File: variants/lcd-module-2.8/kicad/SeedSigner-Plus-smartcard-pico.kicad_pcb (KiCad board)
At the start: 2 copper layers, 137.9 x 108.6 mm, 58 parts, among them J301 TYPE-C 6P(073), J302 Conn_01x02_Pin, J401 62684-402100ALF, J601 7312P0225A13LF, J701 Pico-ResTouch-LCD-2.8, Q401 AO3400A, SW501 TS-1101-C-W, SW502 TS-1101-C-W, SW503 TS-1101-C-W, SW504 TS-1101-C-W, SW505 TS-1101-C-W, SW506 TS-1101-C-W, SW507 TS-1101-C-W, SW508 TS-1101-C-W, U202 LuckFox_Pico_MINI, U601 SEC1210/PV-UR2

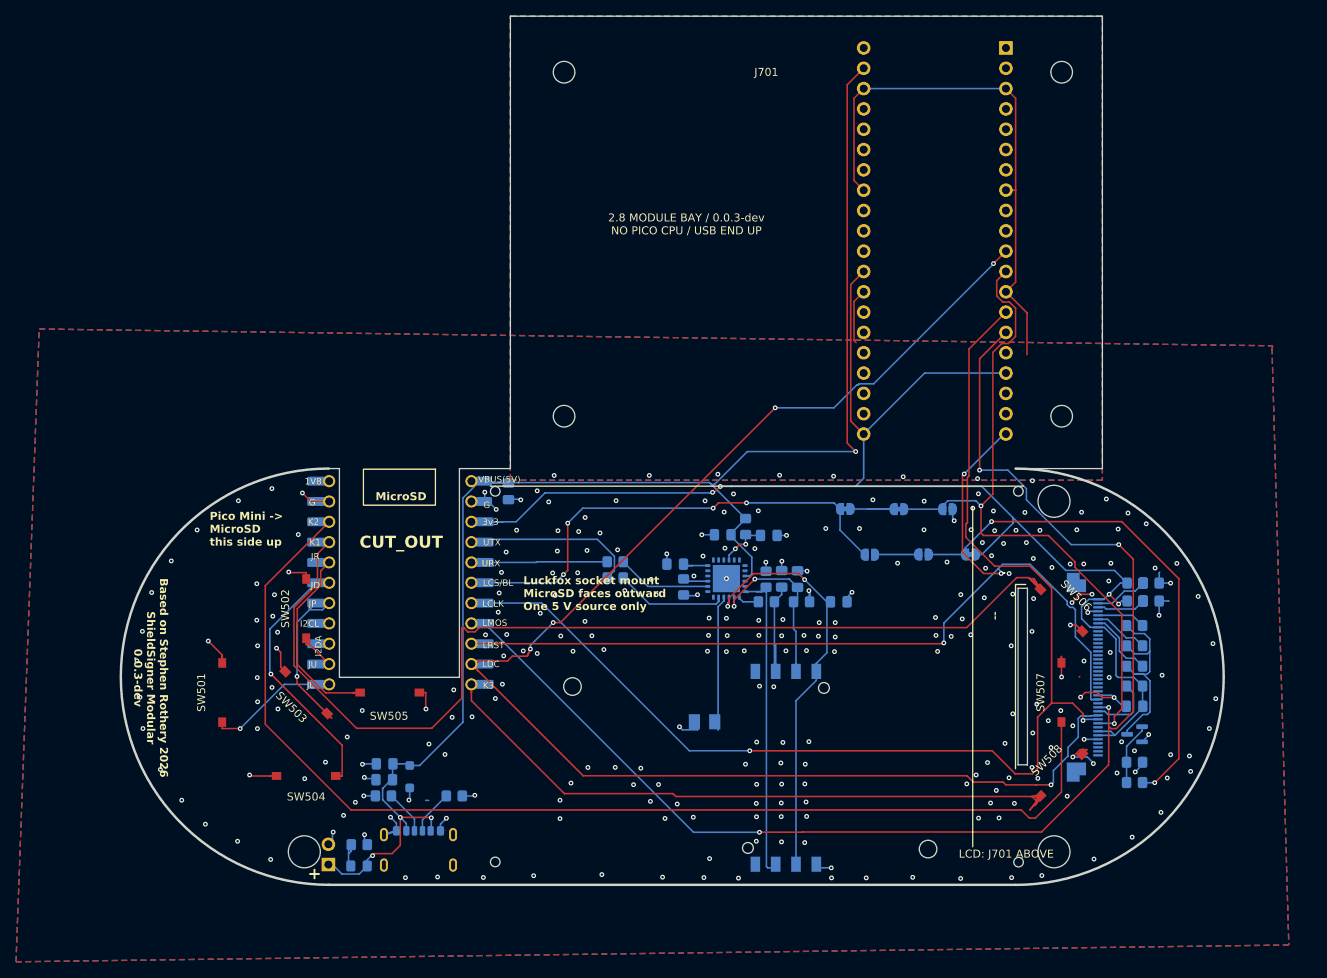
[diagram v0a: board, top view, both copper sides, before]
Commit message: Rebuild modular signer as an eight-pin 2.8-inch pill carrier
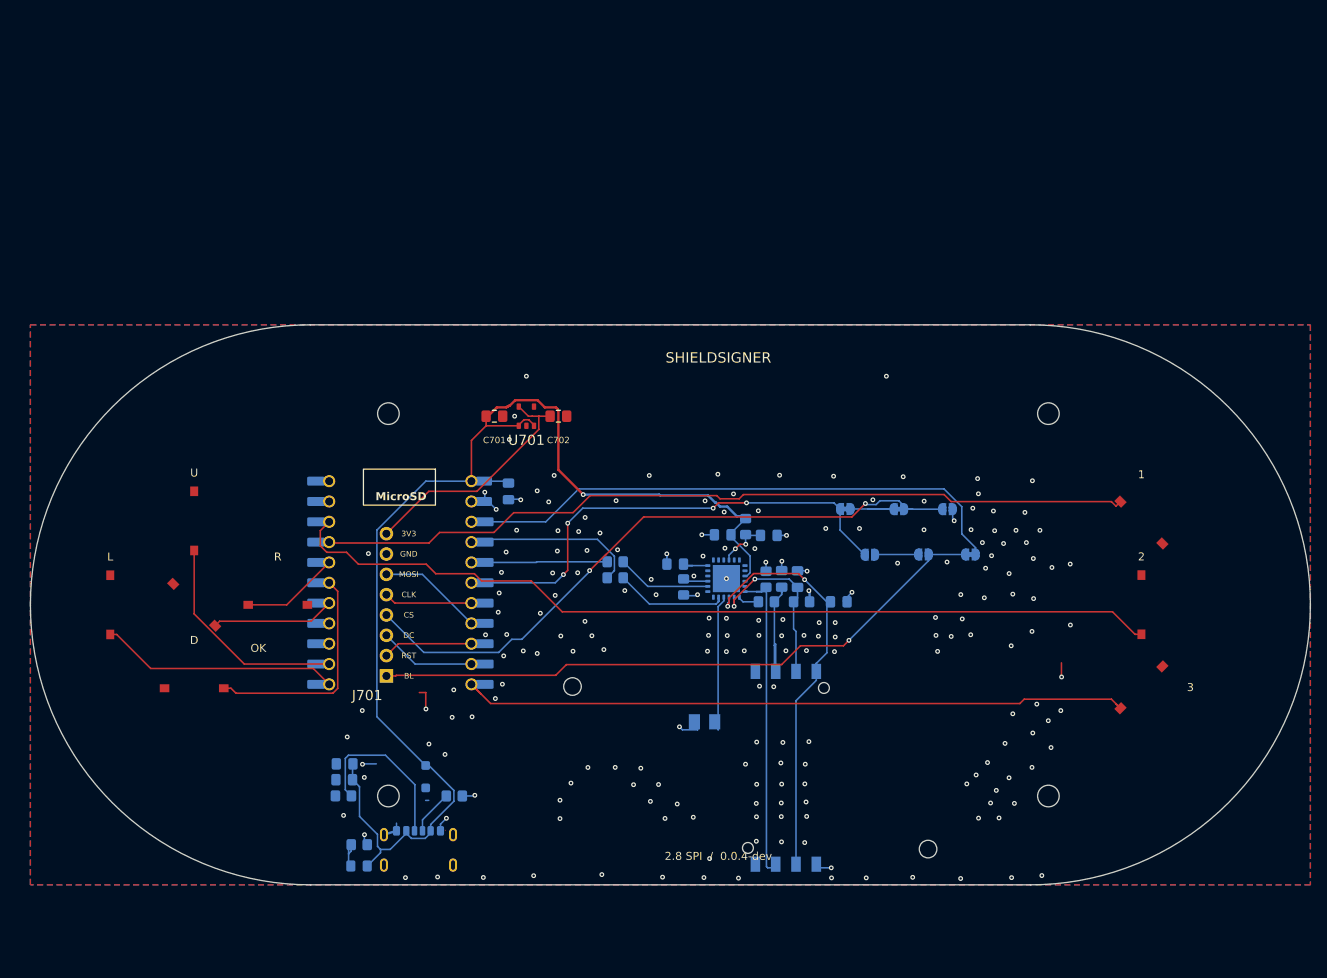
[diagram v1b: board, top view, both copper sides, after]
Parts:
- removed C401: 100n, Capacitor_SMD:C_0805_2012Metric_Pad1.18x1.45mm_HandSolder
- removed J302: Conn_01x02_Pin, Connector_PinSocket_2.54mm:PinSocket_1x02_P2.54mm_Vertical
- removed J401: 62684-402100ALF, Seedsigner-plus-library:AMPHENOL_62684-402100ALF
- removed Q401: AO3400A, Package_TO_SOT_SMD:SOT-23
- removed R401: 330R, Resistor_SMD:R_0805_2012Metric_Pad1.20x1.40mm_HandSolder
- removed R402: 33k, Resistor_SMD:R_0805_2012Metric_Pad1.20x1.40mm_HandSolder
- removed R403, R404, R408, R409: 0R, Resistor_SMD:R_0805_2012Metric_Pad1.20x1.40mm_HandSolder
- removed R405, R406, R407: 47R, Resistor_SMD:R_0805_2012Metric_Pad1.20x1.40mm_HandSolder
- removed R410: 10K, Resistor_SMD:R_0805_2012Metric_Pad1.20x1.40mm_HandSolder
- added C701: 10uF, Capacitor_SMD:C_0805_2012Metric_Pad1.18x1.45mm_HandSolder, F.Cu at (106.0, 66.0)
- added C702: 10uF, Capacitor_SMD:C_0805_2012Metric_Pad1.18x1.45mm_HandSolder, F.Cu at (114.0, 66.0)
- added U701: AP2112K-3.3TRG1, ShieldSigner:AP2112K_SOT25_reflow, F.Cu at (110.0, 66.0)
- H701, H702, H703, H704: footprint MountingHole_2.7mm_M2.5 -> MountingHole:MountingHole_2.7mm_M2.5
- J701: value Pico-ResTouch-LCD-2.8 -> LCD SPI 8-pin; footprint ShieldSigner:Waveshare_Pico_ResTouch_LCD_2.8_Header -> ShieldSigner:LCD_SPI_8_Pill
- moved J701 98.6 mm to (92.5, 98.5)
- moved H703 52.3 mm to (92.8, 113.5)
- moved H701 48.0 mm to (92.8, 65.7)
- moved H704 47.5 mm to (175.2, 113.5)
- moved H702 42.7 mm to (175.2, 65.7)
- moved SW501 17.8 mm to (58.0, 89.6)
- moved SW502 17.8 mm to (68.5, 79.1)
- moved SW503 17.8 mm to (68.5, 89.6)
- moved SW504 17.8 mm to (68.5, 100.0)
- moved SW505 17.8 mm to (78.9, 89.6)
- moved SW506 14.8 mm to (186.9, 79.3)
- moved SW507 14.8 mm to (186.9, 89.6)
- moved SW508 14.8 mm to (186.9, 99.9)
- moved C301 5.00 mm to (87.2, 111.4)
- moved C302 5.00 mm to (87.3, 109.5)
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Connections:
- J701 pad 1: unconnected-(J701-NC-Pad1) -> RPI_BACKLIGHT
- J701 pad 2: unconnected-(J701-NC-Pad2) -> LCD_RST
- J701 pad 3: GND -> LCD_DC
- J701 pad 4: unconnected-(J701-NC-Pad4) -> RPI_SPI_CS
- J701 pad 5: unconnected-(J701-NC-Pad5) -> LCD_SCLK
- J701 pad 6: unconnected-(J701-NC-Pad6) -> LCD_MOSI
- J701 pad 7: unconnected-(J701-NC-Pad7) -> GND
- J701 pad 8: GND -> LCD_3V3
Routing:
- net LCD_DC: track 183.1 -> 13.8 mm, vias 5 -> 0
- net LCD_MOSI: track 169.6 -> 14.8 mm, vias 4 -> 0
- net LCD_SCLK: track 154.1 -> 12.7 mm, vias 2 -> 0
- net GND: track 175.4 -> 39.6 mm, vias 283 -> 206
- net +3.3V: track 186.2 -> 71.0 mm, vias 4 -> 0
- net LCD_RST: track 122.1 -> 12.9 mm, vias 3 -> 0
- net Key1: track 146.2 -> 104.3 mm
- net +5V: track 192.3 -> 154.0 mm, vias 4 -> 1
- net Key2: track 144.7 -> 112.3 mm
- net LCD_3V3: track 0.00 -> 30.5 mm
- net Net-(Q401-D): track 26.1 -> 0.00 mm
- net JoystickUp: track 8.14 -> 29.0 mm
- net Net-(J301-CC2): track 5.56 -> 21.4 mm
- net JoystickLeft: track 16.5 -> 31.6 mm, vias 1 -> 0
- net RPI_BACKLIGHT: track 65.1 -> 79.1 mm, vias 2 -> 1
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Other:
- board size 137.9 x 108.6 mm -> 160 x 70 mm
- board text added: "1"
- board text added: "12 mm LCD supports"
- board text added: "2"
- board text added: "2.8 SPI / 0.0.4-dev"
- board text added: "3"
- board text added: "3V3"
- board text added: "BL"
- board text added: "Based on Stephen Rothery 2026"
- board text added: "CLK"
- board text added: "CS"
- board text added: "D"
- board text added: "DC"
- board text added: "GND"
- board text added: "L"
- board text added: "MOSI"
- board text added: "OK"
- board text added: "R"
- board text added: "RST"
- board text added: "SHIELDSIGNER"
- board text added: "U"

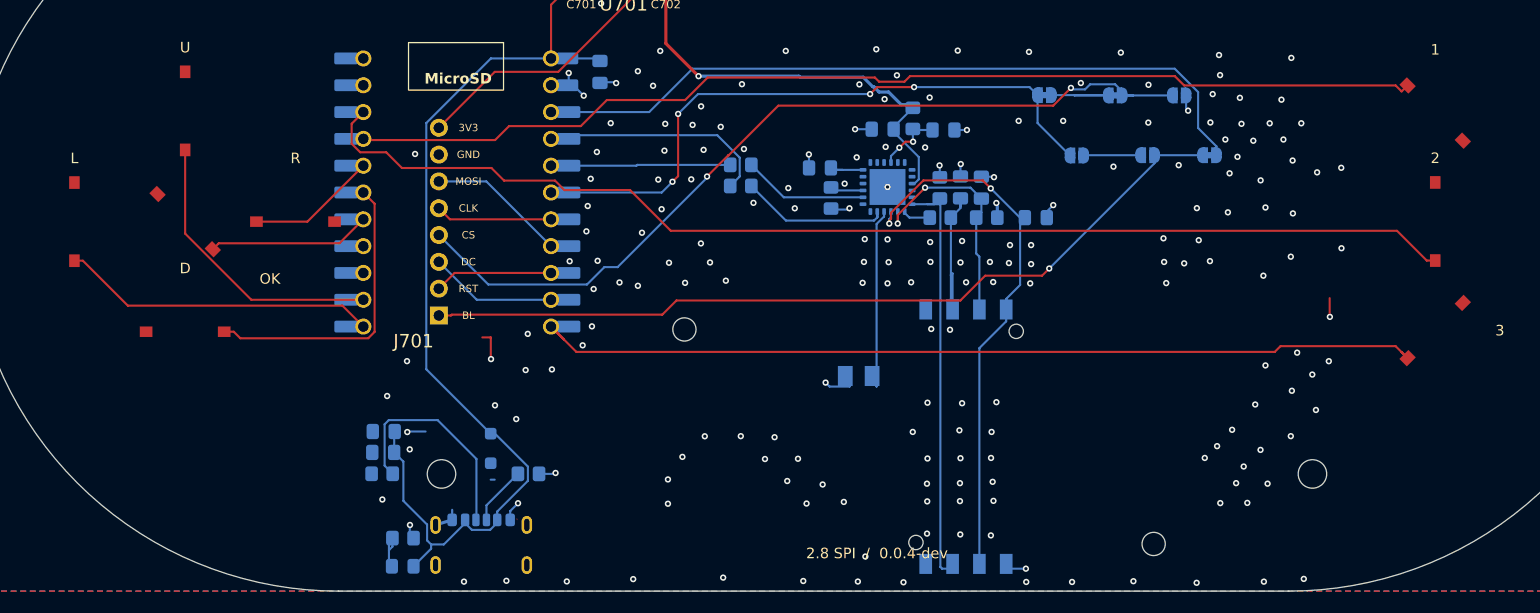
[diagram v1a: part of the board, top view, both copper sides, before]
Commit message: Revise modular carrier for shared-supplier switches and USB-C
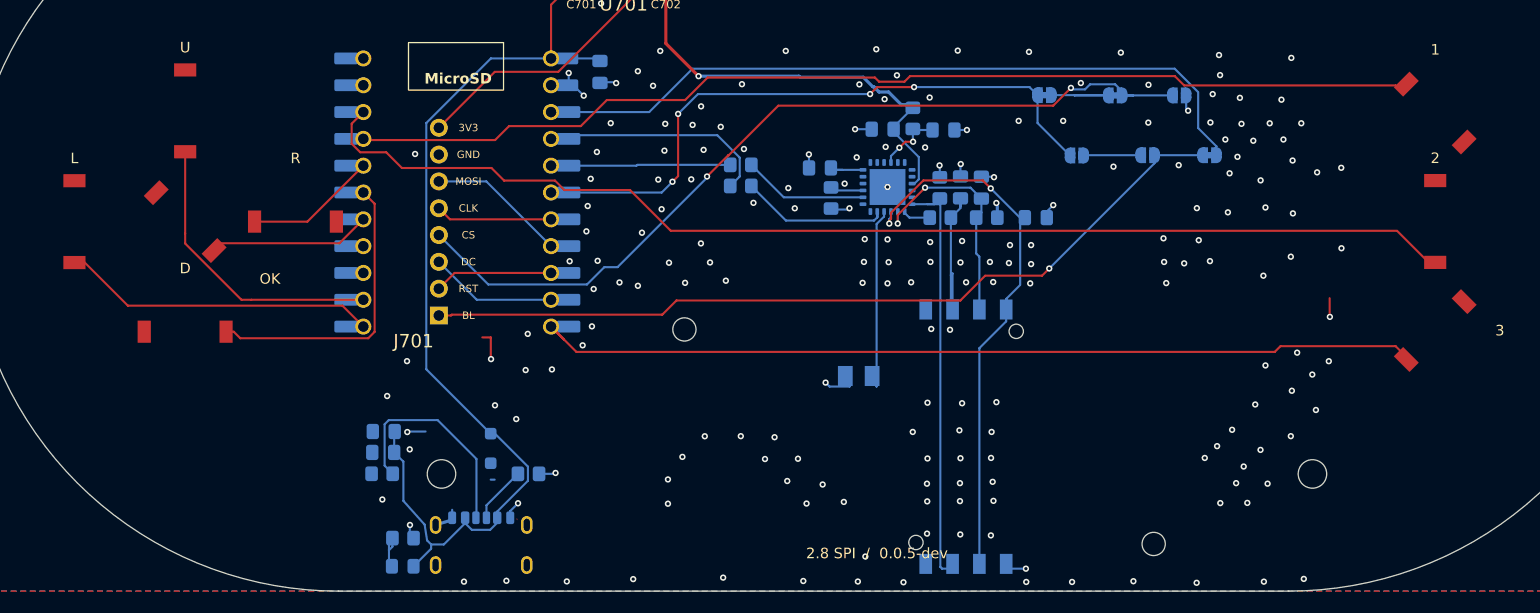
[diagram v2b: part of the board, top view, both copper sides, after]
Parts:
- J301: value TYPE-C 6P(073) -> USB4125-GF-A; footprint ShieldSigner:SHOUHAN_TYPE_C_6P_073 -> ShieldSigner:GCT_USB4125_GF_A
- SW501, SW502, SW503, SW504, SW505, SW506, SW507, SW508: value TS-1101-C-W -> PTS636SK25SMTRLFS; footprint ShieldSigner:XKB_TS1101_C_W_reflow -> ShieldSigner:CK_PTS636_SK25_G
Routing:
- net JoystickUp: track 29.0 -> 29.6 mm
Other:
- board text added: "2.8 SPI / 0.0.5-dev"
- board text removed: "2.8 SPI / 0.0.4-dev"

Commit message: Add alternate 5V power header and complete USB-C assembly sourcing
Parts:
- added J302: 5V_IN, ShieldSigner:PowerHeader_1x02_P2.54mm, F.Cu at (105.0, 120.0)
- J301: value USB4125-GF-A -> USB4125-GF-A-0190
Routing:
- net +5V: track 153.8 -> 162.8 mm, vias 1 -> 2
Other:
- board text added: "2.8 SPI / 0.0.6-dev"
- board text added: "5V"
- board text removed: "2.8 SPI / 0.0.5-dev"

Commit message: Relocate smartcard support circuit and add probe pads and PCB branding
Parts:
- added TP801: 5V, ShieldSigner:TestPoint_D1.2mm, B.Cu at (99.5, 111.4)
- added TP802: 3V3, ShieldSigner:TestPoint_D1.2mm, B.Cu at (133.4, 75.1)
- added TP803: LCD3V3, ShieldSigner:TestPoint_D1.2mm, F.Cu at (99.8, 75.4)
- added TP804: GND, ShieldSigner:TestPoint_D1.2mm, B.Cu at (113.6, 88.4)
- added TP805: SC VCC, ShieldSigner:TestPoint_D1.2mm, B.Cu at (151.4, 71.1)
- added TP806: UART RX, ShieldSigner:TestPoint_D1.2mm, B.Cu at (124.3, 69.4)
- added TP807: UART TX, ShieldSigner:TestPoint_D1.2mm, B.Cu at (125.4, 72.5)
- added TP808: SC CLK, ShieldSigner:TestPoint_D1.2mm, B.Cu at (145.8, 74.1)
- added TP809: SC IO, ShieldSigner:TestPoint_D1.2mm, B.Cu at (137.9, 73.7)
- added TP810: CARD DET, ShieldSigner:TestPoint_D1.2mm, B.Cu at (161.6, 88.9)
- added TP811: SC RST, ShieldSigner:TestPoint_D1.2mm, B.Cu at (147.5, 85.1)
- added TP812: GND, ShieldSigner:TestPoint_D1.2mm, B.Cu at (103.6, 113.4)
- moved C601 17.0 mm to (140.3, 63.9)
- moved C602 17.0 mm to (134.5, 63.8)
- moved C603 17.0 mm to (128.6, 67.5)
- moved C605 17.0 mm to (143.9, 69.4)
- moved C606 17.0 mm to (141.9, 69.3)
- moved R601 17.0 mm to (137.4, 62.8)
- moved R602 17.0 mm to (121.1, 69.2)
- moved R603 17.0 mm to (121.1, 67.2)
- moved R604 17.0 mm to (140.0, 72.2)
- moved R605 17.0 mm to (144.4, 72.2)
- moved R606 17.0 mm to (140.0, 69.4)
- moved R607 17.0 mm to (129.7, 70.3)
- moved U601 17.0 mm to (135.0, 69.3)
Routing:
- net /Smartcard Interface/SEC1210_SC_PRSNT: track 18.2 -> 92.2 mm, vias 0 -> 4
- net /Smartcard Interface/SEC1210_SC_RST: track 22.5 -> 87.8 mm, vias 2 -> 5
- net /Smartcard Interface/SEC1210_SC_CLK_PostR: track 15.0 -> 71.1 mm, vias 0 -> 2
- net /Smartcard Interface/SEC1210_SC_IO: track 40.4 -> 89.3 mm, vias 0 -> 2
- net /Smartcard Interface/SEC1210_SC_VCC: track 55.2 -> 103.4 mm, vias 2 -> 4
- net +5V: track 162.8 -> 196.7 mm, vias 2 -> 3
- net UART_RX: track 17.0 -> 32.6 mm, vias 0 -> 2
- net UART_TX: track 22.2 -> 28.0 mm
- net GND: vias 206 -> 203
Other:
- board text added: "2.8 SPI / 0.0.7-dev"
- board text added: "5V USB-C"
- board text added: "CARD DET"
- board text added: "LCD3V3"
- board text added: "LightningSpore"
- board text added: "OPEN HARDWARE"
- board text added: "POWER ONLY"
- board text added: "SC CLK"
- board text added: "SC IO"
- board text added: "SC RST"
- board text added: "SC VCC"
- board text added: "ShieldSigner"
- board text added: "UART RX"
- board text added: "UART TX"
- board text added: "shieldsigner.dev"
- board text removed: "2.8 SPI / 0.0.6-dev"
